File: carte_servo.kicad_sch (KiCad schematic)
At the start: 42 parts, among them J16 Conn_01x04_Male, J17 Conn_01x04_Male, J2 Conn_02x04_Top_Bottom, J24 Conn_LEDs, P1 USB_C_Plug_USB2.0, SW1 CK_KMS2xxG, U1 XGZP6897D_differential_pressu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, U2 XGZP6897D_differential_pressu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, U6 SN65HVD230, U7 LD1117S33TR_SOT223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

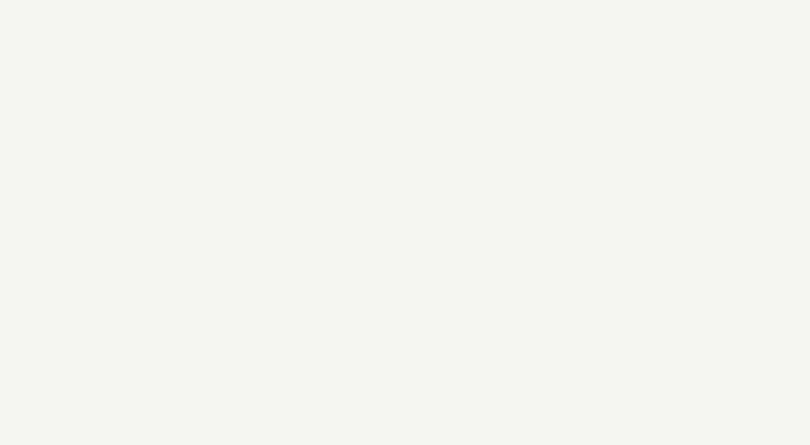
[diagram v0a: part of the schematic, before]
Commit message: add mounting holes
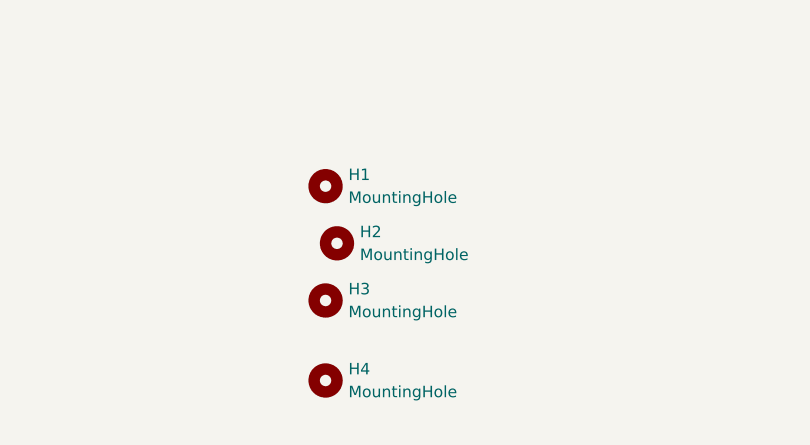
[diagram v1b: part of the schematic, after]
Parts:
- added H1, H2, H3, H4: MountingHole, MountingHole:MountingHole_3.2mm_M3, symbol Mechanical:MountingHole

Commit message: 12V logic for ESP32 + add legends + fine tune
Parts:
- added C31, C32: C, Capacitor_SMD:C_0805_2012Metric, symbol Device:C
- added D8: 13V, Diode_SMD:D_1206_3216Metric, symbol Device:D_Zener
- added F2: Fuse, Fuse:Fuse_Littelfuse-NANO2-451_453, symbol Device:Fuse
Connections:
- net GND_POW is gone; now on net GND: J2.1 (Pin_1), J2.2 (Pin_2)
- net 12V_ELEC_P: now also F2.2; no longer F1.2
- net 12V_POW_P: now also F1.2
- net GND: now also C31.2, C32.2, D8.2 (A)
- new net BATT_12V_elec: C31.1, C32.1, D8.1 (K), F2.1
- no-connect marks 10 -> 8
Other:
- sheet DCDC_5V ports: added Enable_for_DCDC_logic, Vin_for_DCDC_logic; removed Vin, enable

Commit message: fix warnings + add internal layers + add Uart to steppers (TX only
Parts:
- added D10, D9: D, Diode_SMD:D_SOD-882, symbol Device:D
- added R38, R39: 1kR, Resistor_SMD:R_0603_1608Metric, symbol Device:R_Small
- J16, J17: symbol Connector:Conn_01x04_Male -> Connector_Generic:Conn_01x04
- J24: symbol Connector:Conn_01x03_Male -> Connector:Conn_01x03_Pin
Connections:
- net UartToStepper: now reaches U8.31 (GPIO38/FSPIWP/SUBSPIWP)
- net UartToStepper: now also R38.1, R39.2
- new net: D10.2 (A), R39.1
- new net: D9.2 (A), R38.2
- new net stepper_driver/PDN/UART: D9.1 (K)
- new net stepper_driver1/PDN/UART: D10.1 (K)
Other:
- sheet stepper_driver ports: added PDN/UART; removed none
- sheet stepper_driver1 ports: added PDN/UART; removed none
- note added: "Pour contrôler deux steppers d'une seule pin"
- moved on the sheet: J24, R21

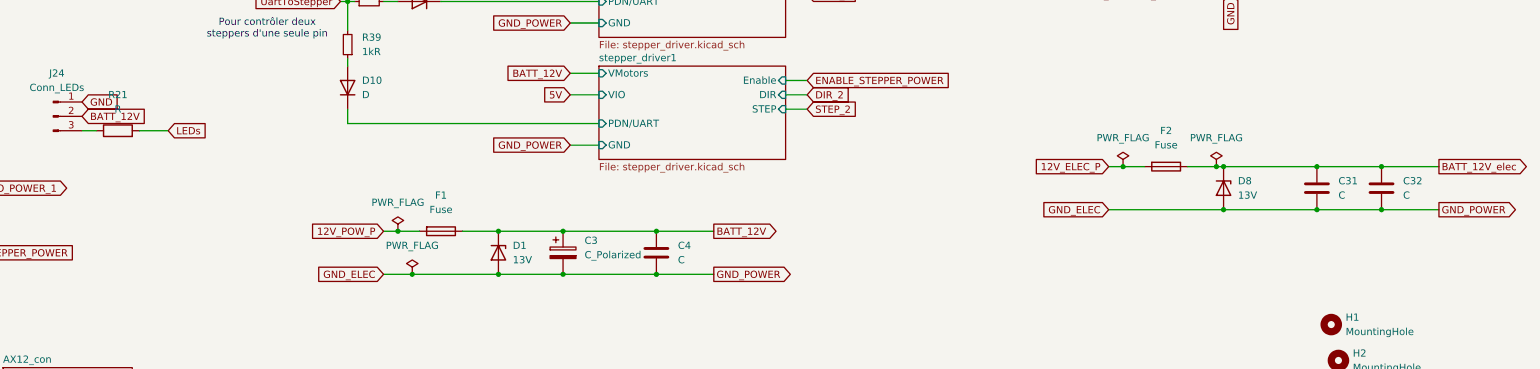
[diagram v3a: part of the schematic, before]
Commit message: export bom as CSV
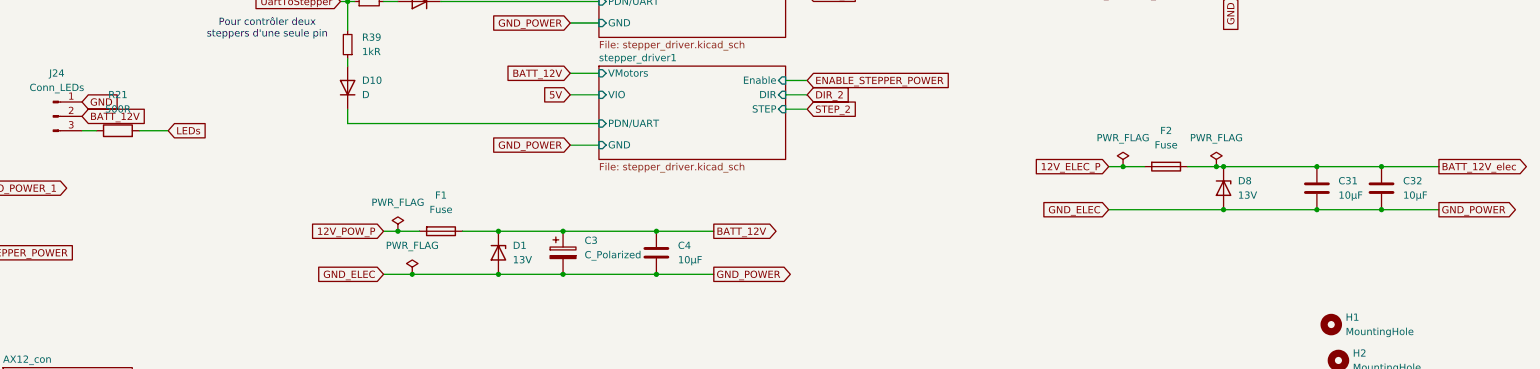
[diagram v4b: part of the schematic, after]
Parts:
- C31, C32, C4: value C -> 10µF
- R21: value R -> 500R
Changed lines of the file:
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@@
 			)
 		)
-		(property "Value" "C"
+		(property "Value" "10µF"
 			(at 374.65 144.7799 0)
 			(effects
@@
 			)
 		)
-		(property "Value" "R"
+		(property "Value" "500R"
 			(at 147.32 129.54 90)
 			(effects
@@
 			)
 		)
-		(property "Value" "C"
+		(property "Value" "10µF"
 			(at 363.22 144.7799 0)
 			(effects
@@
 			)
 		)
-		(property "Value" "C"
+		(property "Value" "10µF"
 			(at 246.38 156.2099 0)
 			(effects

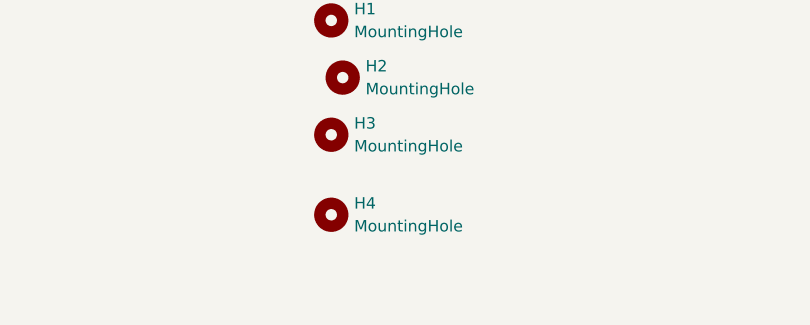
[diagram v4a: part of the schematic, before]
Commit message: add capa for servos
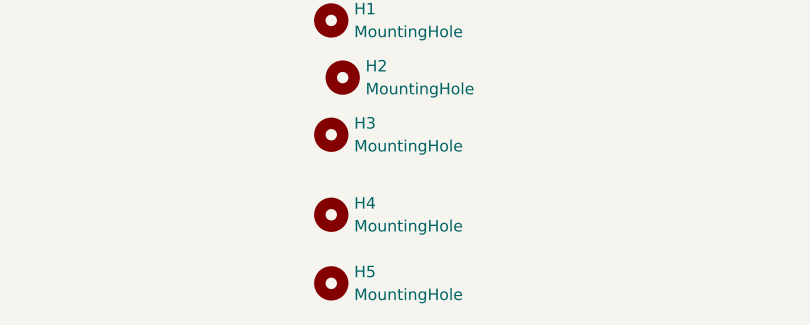
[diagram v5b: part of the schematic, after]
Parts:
- added H5: MountingHole, MountingHole:MountingHole_3.2mm_M3, symbol Mechanical:MountingHole
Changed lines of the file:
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@@
+	)
+	(symbol
+		(lib_id "Mechanical:MountingHole")
+		(at 361.95 196.85 0)
+		(unit 1)
+		(exclude_from_sim yes)
+		(in_bom no)
+		(on_board yes)
+		(dnp no)
+		(fields_autoplaced yes)
+		(property "Reference" "H5"
+			(at 364.49 195.5799 0)
+			(effects
+				(font
+					(size 1.27 1.27)
+				)
+				(justify left)
+			)
+		)
+		(property "Value" "MountingHole"
+			(at 364.49 198.1199 0)
+			(effects
+				(font
+					(size 1.27 1.27)
+				)
+				(justify left)
+			)
+		)
+		(property "Footprint" "MountingHole:MountingHole_3.2mm_M3"
+			(at 361.95 196.85 0)
+			(effects
+				(font
+					(size 1.27 1.27)
+				)
+				(hide yes)
+			)
+		)
+		(property "Datasheet" "~"
+			(at 361.95 196.85 0)
+			(effects
+				(font
+					(size 1.27 1.27)
+				)
+				(hide yes)
+			)
+		)
+		(property "Description" "Mounting Hole without connection"
+			(at 361.95 196.85 0)
+			(effects
+				(font
+					(size 1.27 1.27)
+				)
+				(hide yes)
+			)
+		)
+		(instances
+			(project "carte_servo"
+				(path "/e63e39d7-6ac0-4ffd-8aa3-1841a4541b55"
+					(reference "H5")
+					(unit 1)
+				)
+			)
+		)
 	)
 	(symbol

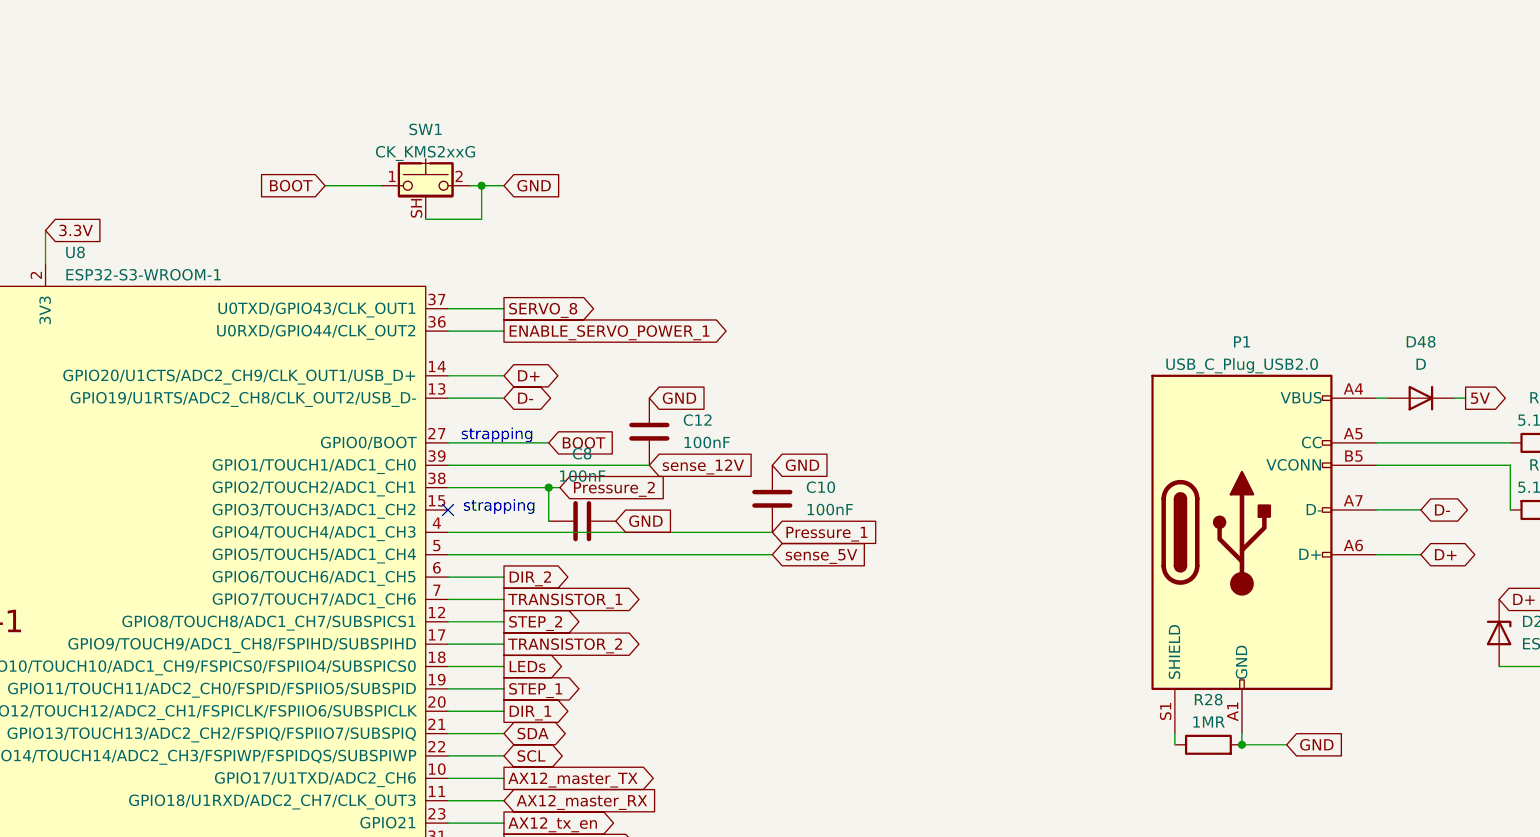
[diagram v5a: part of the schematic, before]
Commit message: fix warnings, change USB-C and button
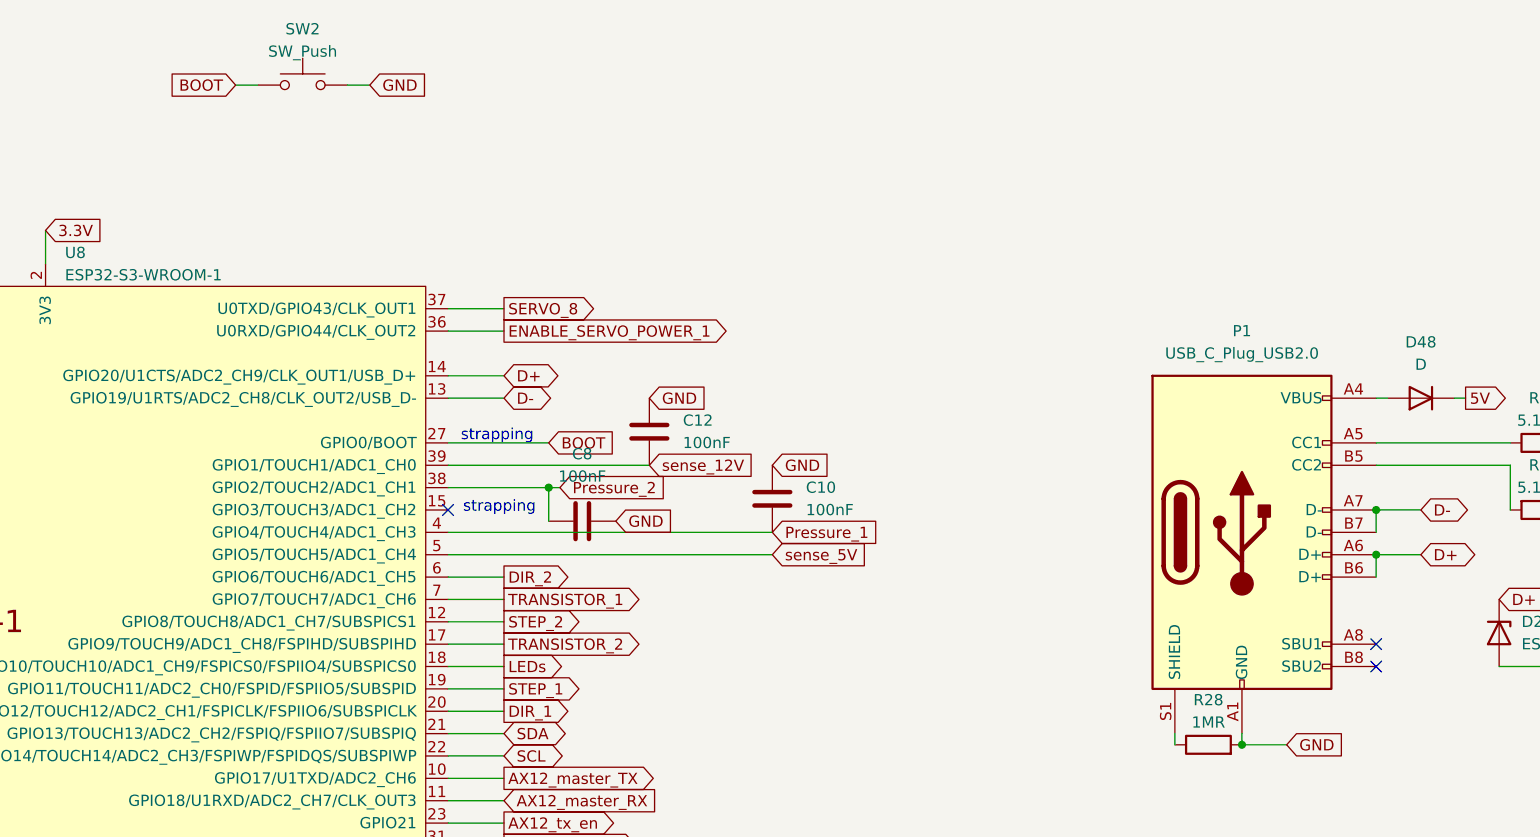
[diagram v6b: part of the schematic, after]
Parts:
- removed SW1: CK_KMS2xxG, Button_Switch_SMD:SW_SPST_CK_KMS2xxGP, symbol Switch:CK_KMS2xxG
- added SW2: SW_Push, button:BZCN TSA007A1518B03, symbol Switch:SW_Push
- P1: footprint Connector_USB:USB_C_Receptacle_GCT_USB4110 -> USBC:G-Switch GT-USB-7047A; symbol Connector:USB_C_Plug_USB2.0 -> Connector:USB_C_Receptacle_USB2.0_16P
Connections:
- net BOOT: now also SW2.1
- net D+: now also P1.B6 (D+)
- net D-: now also P1.B7 (D-)
- net GND: now also SW2.2
- no-connect marks 8 -> 10
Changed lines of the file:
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@@
 	)
 	(junction
+		(at 593.09 36.83)
+		(diameter 0)
+		(color 0 0 0 0)
+	)
+	(junction
+		(at 593.09 41.91)
+		(diameter 0)
+		(color 0 0 0 0)
+	)
+	(junction
 		(at 323.85 53.34)
 		(diameter 0)
@@
 	)
 	(junction
-		(at 491.49 0)
-		(diameter 0)
-		(color 0 0 0 0)
-	)
-	(junction
 		(at 342.9 147.32)
 		(diameter 0)
@@
 	)
 	(no_connect
+		(at 593.09 52.07)
+	)
+	(no_connect
 		(at 107.95 127)
 	)
@@
 	)
 	(no_connect
+		(at 593.09 54.61)
+	)
+	(no_connect
 		(at 312.42 101.6)
 	)
@@
 	(wire
 		(pts
-			(xy 491.49 3.81) (xy 491.49 0)
-		)
-		(stroke
-			(width 0)
-			(type default)
-		)
-	)
-	(wire
-		(pts
 			(xy 593.09 41.91) (xy 598.17 41.91)
 		)
@@
 	(wire
 		(pts
-			(xy 494.03 0) (xy 491.49 0)
-		)
-		(stroke
-			(width 0)
-			(type default)
-		)
-	)
-	(wire
-		(pts
 			(xy 106.68 182.88) (xy 106.68 185.42)
 		)
@@
 	(wire
 		(pts
+			(xy 593.09 41.91) (xy 593.09 44.45)
+		)
+		(stroke
+			(width 0)
+			(type default)
+		)
+	)
+	(wire
+		(pts
 			(xy 93.98 86.36) (xy 85.09 86.36)
 		)
@@
 	(wire
 		(pts
-			(xy 473.71 0) (xy 480.06 0)
+			(xy 335.28 60.96) (xy 344.17 60.96)
 		)
 		(stroke
@@
 	(wire
 		(pts
-			(xy 335.28 60.96) (xy 344.17 60.96)
+			(xy 478.79 -11.43) (xy 476.25 -11.43)
 		)
 		(stroke
@@
 	(wire
 		(pts
-			(xy 485.14 3.81) (xy 491.49 3.81)
-		)
-		(stroke
-			(width 0)
-			(type default)
-		)
-	)
-	(wire
-		(pts
 			(xy 187.96 110.49) (xy 189.23 110.49)
 		)
@@
 	(wire
 		(pts
-			(xy 491.49 0) (xy 490.22 0)
-		)
-		(stroke
-			(width 0)
-			(type default)
-		)
-	)
-	(wire
-		(pts
 			(xy 229.87 53.34) (xy 210.82 53.34)
 		)
@@
 	(wire
 		(pts
+			(xy 593.09 36.83) (xy 593.09 39.37)
+		)
+		(stroke
+			(width 0)
+			(type default)
+		)
+	)
+	(wire
+		(pts
 			(xy 149.86 184.15) (xy 153.67 184.15)
 		)
@@
 	(wire
 		(pts
+			(xy 463.55 -11.43) (xy 466.09 -11.43)
+		)
+		(stroke
+			(width 0)
+			(type default)
+		)
+	)
+	(wire
+		(pts
 			(xy 54.61 66.04) (xy 59.69 66.04)
 		)
@@
 		)
 	)
-	(global_label "GND"
-		(shape input)
-		(at 494.03 0 0)
-		(fields_autoplaced yes)
-		(effects
-			(font
-				(size 1.27 1.27)
-			)
-			(justify left)
-		)
-		(property "Intersheetrefs" "${INTERSHEET_REFS}"
-			(at 500.8857 0 0)
-			(effects
-				(font
-					(size 1.27 1.27)
-				)
-				(justify left)
-				(hide yes)
-			)
-		)
-	)
 	(global_label "SERVO_7"
 		(shape output)
@@
 		)
 	)
+	(global_label "GND"
+		(shape input)
+		(at 478.79 -11.43 0)
+		(fields_autoplaced yes)
+		(effects
+			(font
+				(size 1.27 1.27)
+			)
+			(justify left)
+		)
+		(property "Intersheetrefs" "${INTERSHEET_REFS}"
+			(at 485.6457 -11.43 0)
+			(effects
+				(font
+					(size 1.27 1.27)
+				)
+				(justify left)
+				(hide yes)
+			)
+		)
+	)
 	(global_label "CAN+"
 		(shape bidirectional)
@@
 		)
 	)
-	(global_label "BOOT"
-		(shape input)
-		(at 473.71 0 180)
-		(fields_autoplaced yes)
-		(effects
-			(font
-				(size 1.27 1.27)
-			)
-			(justify right)
-		)
-		(property "Intersheetrefs" "${INTERSHEET_REFS}"
-			(at 465.8262 0 0)
-			(effects
-				(font
-					(size 1.27 1.27)
-				)
-				(justify right)
-				(hide yes)
-			)
-		)
-	)
 	(global_label "GND_POWER"
 		(shape input)
@@
 		)
 	)
+	(global_label "BOOT"
+		(shape input)
+		(at 463.55 -11.43 180)
+		(fields_autoplaced yes)
+		(effects
+			(font
+				(size 1.27 1.27)
+			)
+			(justify right)
+		)
+		(property "Intersheetrefs" "${INTERSHEET_REFS}"
+			(at 455.6662 -11.43 0)
+			(effects
+				(font
+					(size 1.27 1.27)
+				)
+				(justify right)
+				(hide yes)
+			)
+		)
+	)
 	(global_label "GND"
 		(shape input)
@@
 	)
 	(symbol
-		(lib_id "Connector:USB_C_Plug_USB2.0")
+		(lib_id "Connector:USB_C_Receptacle_USB2.0_16P")
 		(at 577.85 39.37 0)
 		(unit 1)
@@
 		(fields_autoplaced yes)
 		(property "Reference" "P1"
-			(at 577.85 17.78 0)
+			(at 577.85 16.51 0)
 			(effects
 				(font
@@
 		)
 		(property "Value" "USB_C_Plug_USB2.0"
-			(at 577.85 20.32 0)
+			(at 577.85 19.05 0)
 			(effects
 				(font
@@
 			)
 		)
-		(property "Footprint" "Connector_USB:USB_C_Receptacle_GCT_USB4110"
+		(property "Footprint" "USBC:G-Switch GT-USB-7047A"
 			(at 581.66 39.37 0)
 			(effects
@@
 			)
 		)
-		(property "Description" "USB 2.0-only Type-C Plug connector"
+		(property "Description" "USB 2.0-only 16P Type-C Receptacle connector"
 			(at 577.85 39.37 0)
 			(effects
@@
 		(pin "B1"
 		)
+		(pin "B7"
+		)
+		(pin "A8"
+		)
+		(pin "B8"
+		)
+		(pin "B6"
+		)
 		(instances
 			(project ""
@@
 	)
 	(symbol
-		(lib_id "Switch:CK_KMS2xxG")
-		(at 485.14 0 0)
+		(lib_id "Switch:SW_Push")
+		(at 471.17 -11.43 0)
 		(unit 1)
 		(exclude_from_sim no)
@@
 		(dnp no)
 		(fields_autoplaced yes)
-		(property "Reference" "SW1"
-			(at 485.14 -6.35 0)
+		(property "Reference" "SW2"
+			(at 471.17 -17.78 0)
 			(effects
 				(font
@@
 			)
 		)
-		(property "Value" "CK_KMS2xxG"
-			(at 485.14 -3.81 0)
+		(property "Value" "SW_Push"
+			(at 471.17 -15.24 0)
 			(effects
 				(font
@@
 			)
 		)
-		(property "Footprint" "Button_Switch_SMD:SW_SPST_CK_KMS2xxGP"
-			(at 485.14 -5.08 0)
+		(property "Footprint" "button:BZCN TSA007A1518B03"
+			(at 471.17 -16.51 0)
 			(effects
 				(font
@@
 			)
 		)
-		(property "Datasheet" "https://www.ckswitches.com/media/1482/kms.pdf"
-			(at 485.14 -5.08 0)
+		(property "Datasheet" "~"
+			(at 471.17 -16.51 0)
 			(effects
 				(font
@@
 			)
 		)
-		(property "Description" "Microminiature SMT Side Actuated, 4.2 x 2.8 x 1.42mm, without pegs, with shield pin"
-			(at 485.14 0 0)
+		(property "Description" "Push button switch, generic, two pins"
+			(at 471.17 -11.43 0)
 			(effects
 				(font
@@
 			)
 		)
-		(pin "SH"
+		(pin "1"
 		)
 		(pin "2"
 		)
-		(pin "1"
-		)
 		(instances
 			(project ""
 				(path "/e63e39d7-6ac0-4ffd-8aa3-1841a4541b55"
-					(reference "SW1")
+					(reference "SW2")
 					(unit 1)
 				)

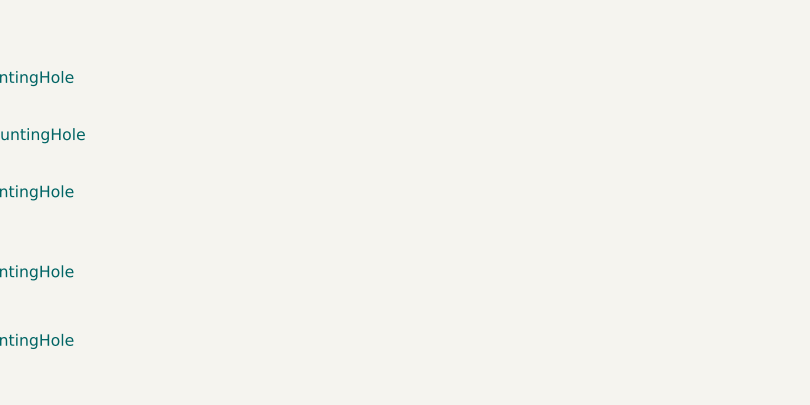
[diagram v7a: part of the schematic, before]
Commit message: add registration holes
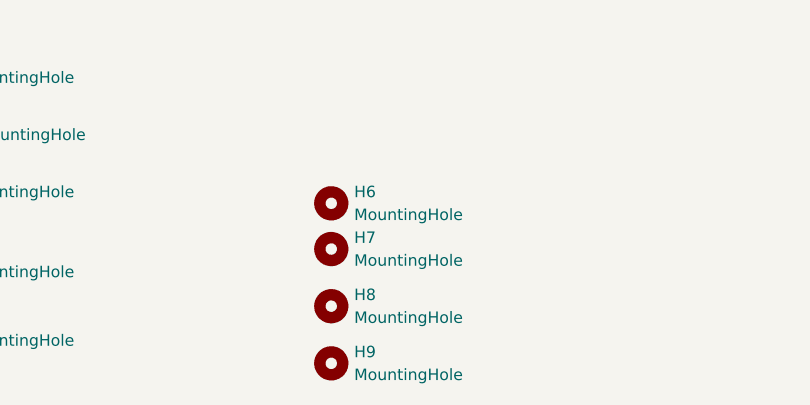
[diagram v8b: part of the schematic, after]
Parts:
- added H6, H7: MountingHole, MountingHole:MountingHole_3mm, symbol Mechanical:MountingHole
- added H8, H9: MountingHole, MountingHole:MountingHole_5mm, symbol Mechanical:MountingHole
